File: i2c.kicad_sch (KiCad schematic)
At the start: 13 parts, among them U12 PCA9306D_118, U13 M24C64-FMC6TG

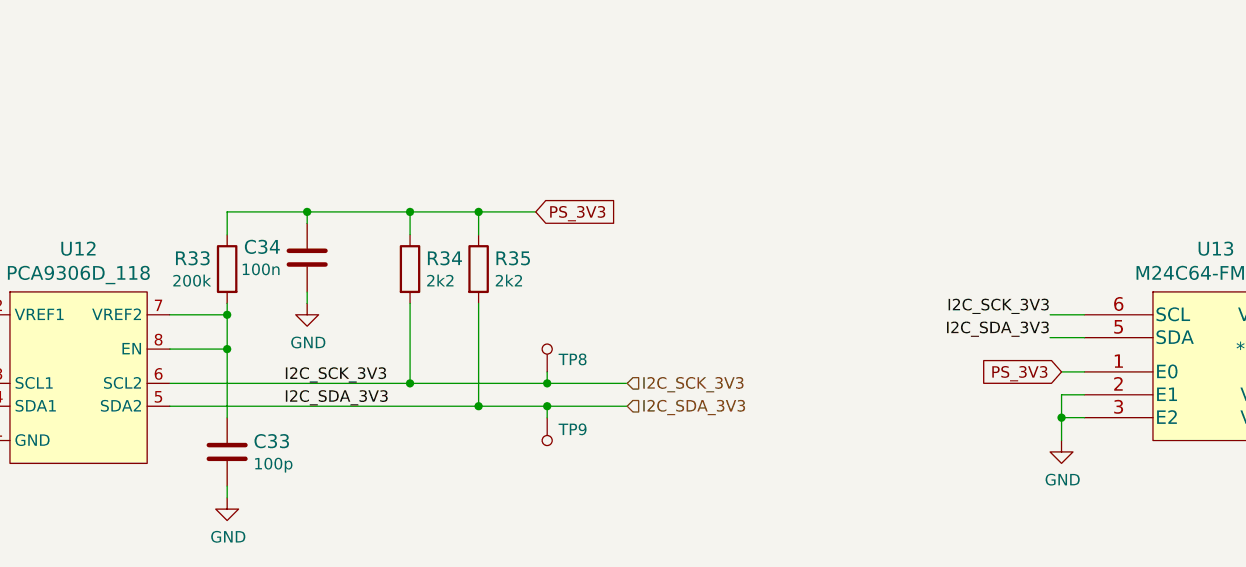
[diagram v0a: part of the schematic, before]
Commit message: Added cosmetic changes to schematics (e.g. position of labels, designators)
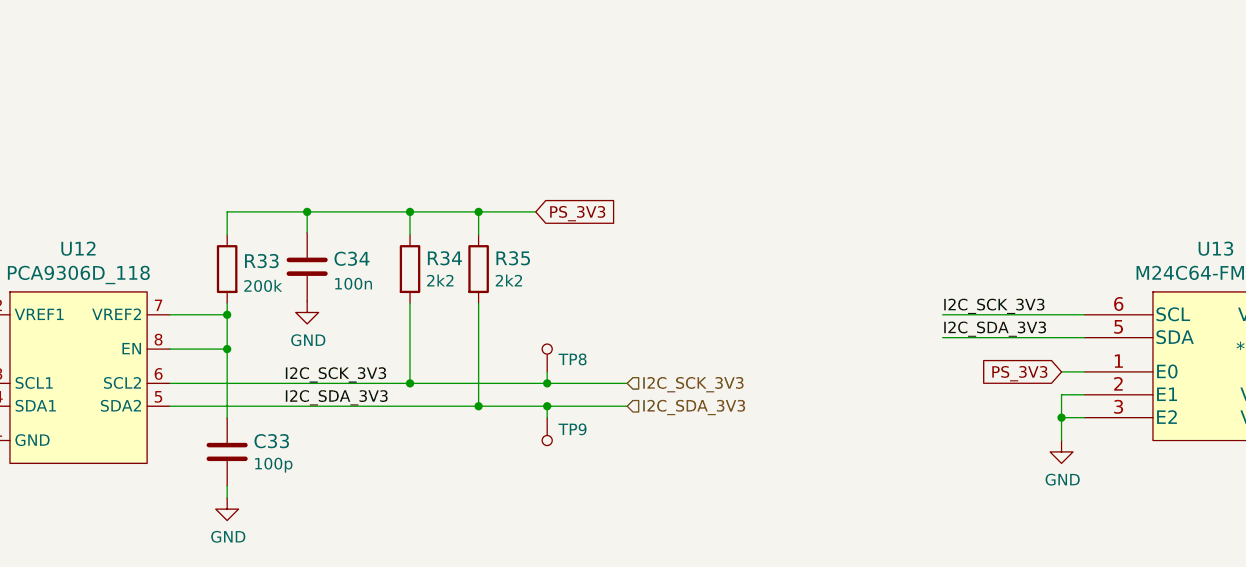
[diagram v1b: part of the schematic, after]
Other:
- moved on the sheet: C34
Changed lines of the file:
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@@
     (stroke (width 0) (type default) (color 0 0 0 0))
   )
-  (wire (pts (xy 184.15 86.36) (xy 187.96 86.36))
+  (wire (pts (xy 172.212 86.36) (xy 187.96 86.36))
     (stroke (width 0) (type default) (color 0 0 0 0))
   )
@@
     (stroke (width 0) (type default) (color 0 0 0 0))
   )
-  (wire (pts (xy 184.15 88.9) (xy 187.96 88.9))
+  (wire (pts (xy 172.212 88.9) (xy 187.96 88.9))
     (stroke (width 0) (type default) (color 0 0 0 0))
   )
@@
     (stroke (width 0) (type default) (color 0 0 0 0))
   )
-  (wire (pts (xy 101.6 85.09) (xy 101.6 83.82))
-    (stroke (width 0) (type default) (color 0 0 0 0))
-  )
   (wire (pts (xy 55.88 85.09) (xy 55.88 83.82))
     (stroke (width 0) (type default) (color 0 0 0 0))
   )
-  (wire (pts (xy 101.6 74.93) (xy 101.6 76.2))
+  (wire (pts (xy 101.6 74.93) (xy 101.6 77.216))
     (stroke (width 0) (type default) (color 0 0 0 0))
   )
@@
     (effects (font (size 2.54 2.54) (thickness 0.508) bold) (justify left bottom))
   )
-  (label "I2C_SCK_3V3" (at 184.15 86.36 180)
-    (effects (font (size 1.27 1.27)) (justify right bottom))
-  )
-  (label "I2C_SDA_3V3" (at 184.15 88.9 180)
-    (effects (font (size 1.27 1.27)) (justify right bottom))
+  (label "I2C_SCK_3V3" (at 172.212 86.36 0)
+    (effects (font (size 1.27 1.27)) (justify left bottom))
+  )
+  (label "I2C_SDA_3V3" (at 172.212 88.9 0)
+    (effects (font (size 1.27 1.27)) (justify left bottom))
   )
   (label "I2C_SDA_3V3" (at 99.06 96.52 0)
@@
     (pin "1")
   )
-  (symbol (lib_id "kria-k26-devboard:C_100n_0402") (at 101.6 80.01 0) (mirror y) (unit 1)
-    (in_bom yes) (on_board yes)
-    (property "Reference" "C34" (id 0) (at 98.679 78.867 0)
-      (effects (font (size 1.524 1.524)) (justify left))
-    )
-    (property "Value" "C_100n_0402" (id 1) (at 101.6 83.82 0)
+  (symbol (lib_id "kria-k26-devboard:C_100n_0402") (at 101.6 81.026 0) (mirror y) (unit 1)
+    (in_bom yes) (on_board yes) (fields_autoplaced)
+    (property "Reference" "C34" (id 0) (at 104.521 80.1914 0)
+      (effects (font (size 1.524 1.524)) (justify right))
+    )
+    (property "Value" "C_100n_0402" (id 1) (at 101.6 84.836 0)
       (effects (font (size 1.524 1.524)) hide)
     )
-    (property "Footprint" "kria-k26-devboard-footprints:0402-cap" (id 2) (at 96.52 74.93 0)
+    (property "Footprint" "kria-k26-devboard-footprints:0402-cap" (id 2) (at 96.52 75.946 0)
       (effects (font (size 1.524 1.524)) (justify left) hide)
     )
-    (property "Datasheet" "" (id 3) (at 101.6 80.01 0)
+    (property "Datasheet" "" (id 3) (at 101.6 81.026 0)
       (effects (font (size 1.27 1.27)) hide)
     )
-    (property "Manufacturer" "Murata" (id 4) (at 96.52 69.85 0)
+    (property "Manufacturer" "Murata" (id 4) (at 96.52 70.866 0)
       (effects (font (size 1.524 1.524)) (justify left) hide)
     )
-    (property "MPN" "GRM155R61H104KE14D" (id 5) (at 96.52 72.39 0)
+    (property "MPN" "GRM155R61H104KE14D" (id 5) (at 96.52 73.406 0)
       (effects (font (size 1.524 1.524)) (justify left) hide)
     )
-    (property "Val" "100n" (id 6) (at 98.679 81.3562 0)
-      (effects (font (size 1.27 1.27)) (justify left))
+    (property "Val" "100n" (id 6) (at 104.521 82.9565 0)
+      (effects (font (size 1.27 1.27)) (justify right))
     )
     (pin "1")
     (pin "2")
   )
-  (symbol (lib_id "kria-k26-devboard:GND") (at 101.6 85.09 0) (unit 1)
+  (symbol (lib_id "kria-k26-devboard:GND") (at 101.6 84.836 0) (unit 1)
     (in_bom yes) (on_board yes)
-    (property "Reference" "#PWR059" (id 0) (at 101.6 91.44 0)
+    (property "Reference" "#PWR059" (id 0) (at 101.6 91.186 0)
       (effects (font (size 1.27 1.27)) hide)
     )
-    (property "Value" "GND" (id 1) (at 101.727 89.4842 0))
-    (property "Footprint" "kria-k26-devboard-footprints:" (id 2) (at 101.6 85.09 0)
+    (property "Value" "GND" (id 1) (at 101.727 89.2302 0))
+    (property "Footprint" "kria-k26-devboard-footprints:" (id 2) (at 101.6 84.836 0)
       (effects (font (size 1.27 1.27)) hide)
     )
-    (property "Datasheet" "" (id 3) (at 101.6 85.09 0)
+    (property "Datasheet" "" (id 3) (at 101.6 84.836 0)
       (effects (font (size 1.27 1.27)) hide)
     )
@@
   )
   (symbol (lib_id "kria-k26-devboard:R_200k_0402") (at 92.71 81.28 90) (mirror x) (unit 1)
-    (in_bom yes) (on_board yes)
-    (property "Reference" "R33" (id 0) (at 90.932 80.137 90)
-      (effects (font (size 1.524 1.524)) (justify left))
+    (in_bom yes) (on_board yes) (fields_autoplaced)
+    (property "Reference" "R33" (id 0) (at 94.488 80.4454 90)
+      (effects (font (size 1.524 1.524)) (justify right))
     )
     (property "Value" "R_200k_0402" (id 1) (at 96.52 81.28 0)
@@
       (effects (font (size 1.524 1.524)) (justify left) hide)
     )
-    (property "Val" "200k" (id 6) (at 90.932 82.6262 90)
-      (effects (font (size 1.27 1.27)) (justify left))
+    (property "Val" "200k" (id 6) (at 94.488 83.2105 90)
+      (effects (font (size 1.27 1.27)) (justify right))
     )
     (pin "1")

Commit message: Bump date and revision
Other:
- title: I2C -> Kria K26 Devboard
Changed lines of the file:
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@@
   (paper "A4")
   (title_block
-    (title "I2C")
-    (date "2022-07-25")
-    (rev "1.1.0")
+    (title "Kria K26 Devboard")
+    (date "2023-02-15")
+    (rev "1.1.1")
     (comment 1 "www.antmicro.com")
     (comment 2 "Antmicro Ltd.")

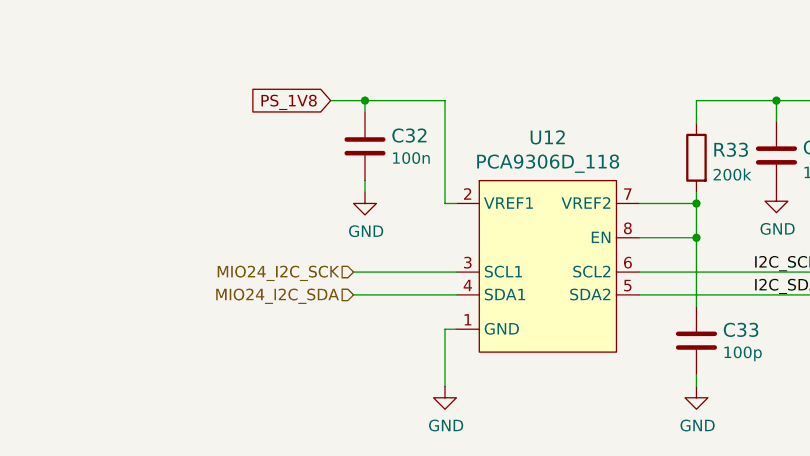
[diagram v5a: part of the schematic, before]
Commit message: Add test point for I2C, fix MIO25_I2C_SDA naming on i2c sheet
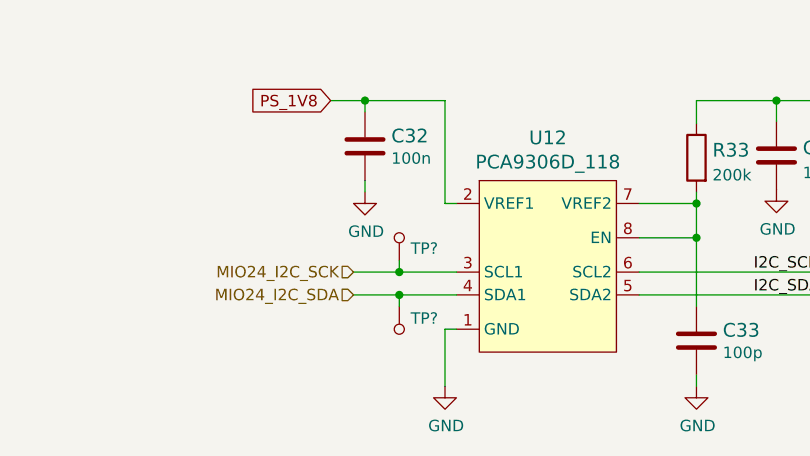
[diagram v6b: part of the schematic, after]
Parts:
- added TP? (x2): TP_SMD_0_75MM, kria-k26-devboard-footprints:Testpoint_smd_0_75mm, symbol kria-k26-devboard:TP_SMD_0_75MM
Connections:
- net MIO24_I2C_SCK: now also TP?.1
- net MIO24_I2C_SDA: now also TP?.1

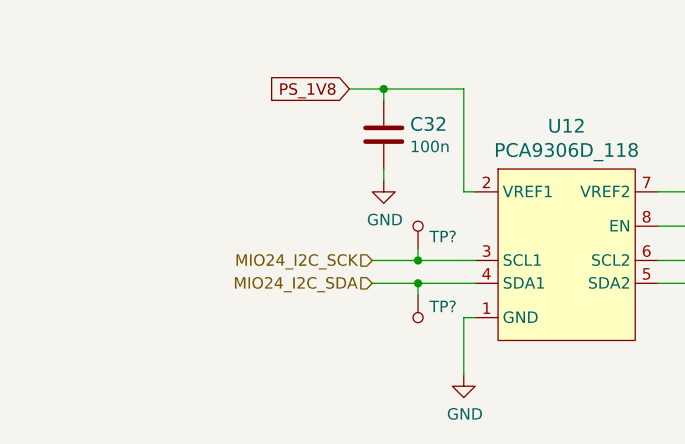
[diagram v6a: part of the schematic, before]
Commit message: Add mandatory pullup to TPS2116 status signal
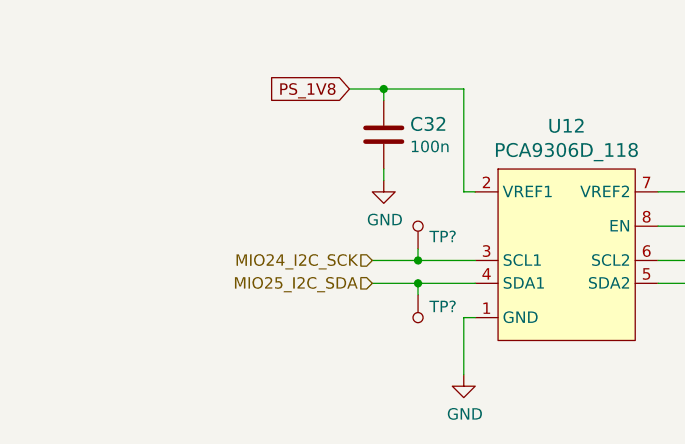
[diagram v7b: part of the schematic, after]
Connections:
- net MIO24_I2C_SDA renamed MIO25_I2C_SDA
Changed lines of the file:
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@@
     (effects (font (size 1.27 1.27)) (justify right))
   )
-  (hierarchical_label "MIO24_I2C_SDA" (shape input) (at 54.61 96.52 180)
+  (hierarchical_label "MIO25_I2C_SDA" (shape input) (at 54.61 96.52 180)
     (effects (font (size 1.27 1.27)) (justify right))
   )

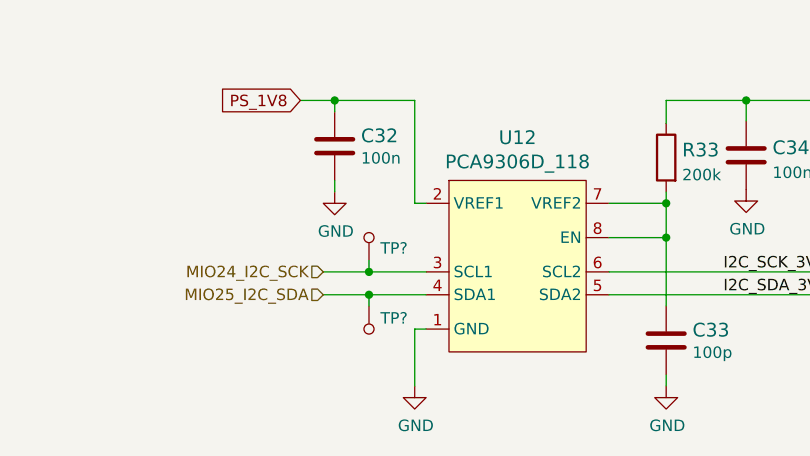
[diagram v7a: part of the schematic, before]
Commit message: Add decoupling to cammera and DP connector, schematic cleanup
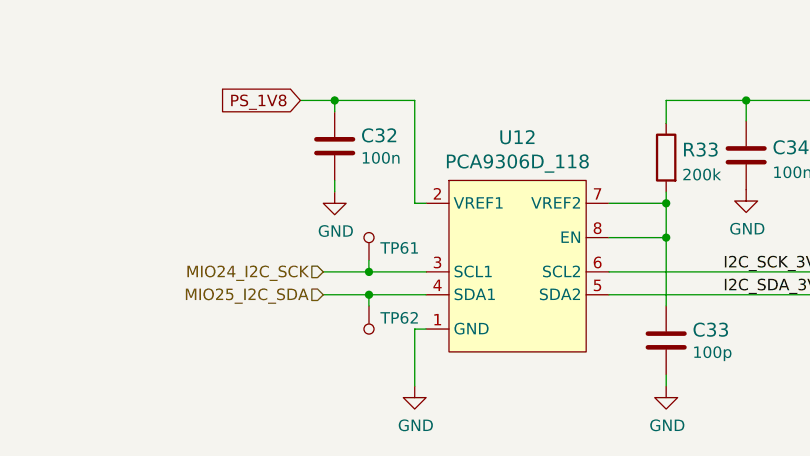
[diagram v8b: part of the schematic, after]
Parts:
- gave numbers to parts that had none: 2
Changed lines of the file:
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@@
   (symbol (lib_id "kria-k26-devboard:TP_SMD_0_75MM") (at 59.69 100.33 0) (unit 1)
     (in_bom yes) (on_board yes)
-    (property "Reference" "TP?" (id 0) (at 60.96 99.1362 0)
+    (property "Reference" "TP62" (id 0) (at 60.96 99.1362 0)
       (effects (font (size 1.27 1.27)) (justify left))
     )
@@
   (symbol (lib_id "kria-k26-devboard:TP_SMD_0_75MM") (at 59.69 90.17 180) (unit 1)
     (in_bom yes) (on_board yes)
-    (property "Reference" "TP?" (id 0) (at 60.96 91.3638 0)
+    (property "Reference" "TP61" (id 0) (at 60.96 91.3638 0)
       (effects (font (size 1.27 1.27)) (justify right))
     )
